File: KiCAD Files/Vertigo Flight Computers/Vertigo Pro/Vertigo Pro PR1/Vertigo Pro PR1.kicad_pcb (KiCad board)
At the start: 4 copper layers, 45.2 x 81.8 mm, 151 parts, among them IC1 ICM-20602, IC2 DPS310XTSA1, J1 ST-LINK Conn, J2 USB_C_2.0, J3 FFC2A32-24-T, J4 Screw_Terminal, J5 Screw_Terminal, J6 Screw_Terminal, J7 Screw_Terminal, Q1 MMBT3904-TP, Q2 MMBT3904-TP, Q3 FDN339AN, Q4 FDN339AN, Q5 SI7149ADP-T1-GE3, Q6 MMBT3904-TP, Q7 MMBT3904-TP, Q8 FDN339AN, Q9 FDN339AN, SW1 SW_SPDT, U1 STM32F103C8Tx, U10 TPS79133DBVR, U12 TLV709, U13 TLV75528PDBV, U2 AP63203WU, U3 ESP32-S3-WROOM-1, U4 TLV75515PDBV, U5 TLV709, U8 NEO-6M-GPS, U9 24AA32A-I_MS, Y1 16MHz

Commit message: Via fix + UART
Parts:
- moved C33 1.03 mm to (144.5, 118.0)
- moved C7 0.26 mm to (142.3, 123.7)
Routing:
- net /ESP_I2C_SCL: track 94.4 -> 84.3 mm, vias 8 -> 7
- net /CONTI_C3: track 30.0 -> 35.3 mm, vias 1 -> 2
- net AGND: track 76.0 -> 80.6 mm, vias 97 -> 95
- net /ULN_3V3: track 31.0 -> 34.0 mm, vias 5 -> 6
- net /STM_UART2_RX: track 26.8 -> 24.5 mm
- net /CONTI_C1: track 25.7 -> 27.9 mm
- net /IGN_4: track 28.8 -> 29.9 mm
- net /CONTI_C4: track 28.5 -> 29.5 mm
- net +3.3V: track 110.1 -> 109.3 mm
- net Net-(Q6-B): track 15.7 -> 16.2 mm
- net /IGN_3: track 47.4 -> 47.6 mm, vias 1 -> 2
- net /ESP_I2C_SDA: track 82.3 -> 82.5 mm, vias 8 -> 7
- net VCC: vias 14 -> 15

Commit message: Via fix, est
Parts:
- removed BOOT, RST: Jumper_2_Open, Jumper:SolderJumper-2_P1.3mm_Open_TrianglePad1.0x1.5mm
- added JP1: Jumper_2_Open, Jumper:SolderJumper-2_P1.3mm_Open_TrianglePad1.0x1.5mm, B.Cu at (151.2, 78.2)
- added JP2: Jumper_2_Open, Jumper:SolderJumper-2_P1.3mm_Open_TrianglePad1.0x1.5mm, B.Cu at (154.1, 78.2)
- moved C34 0.57 mm to (145.5, 117.0)
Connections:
- AE1 pad 2: AGND -> (no net)
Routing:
- net /ULN_3V3: track 34.0 -> 30.8 mm
- net /STM_UART2_TX: track 39.2 -> 36.1 mm
- net +3.3V: track 109.3 -> 107.1 mm, vias 54 -> 53
- net /ESP_I2C_SCL: track 84.3 -> 85.5 mm
- net /ESP_I2C_SDA: track 82.5 -> 83.3 mm
- net AGND: track 80.6 -> 80.5 mm, vias 95 -> 94

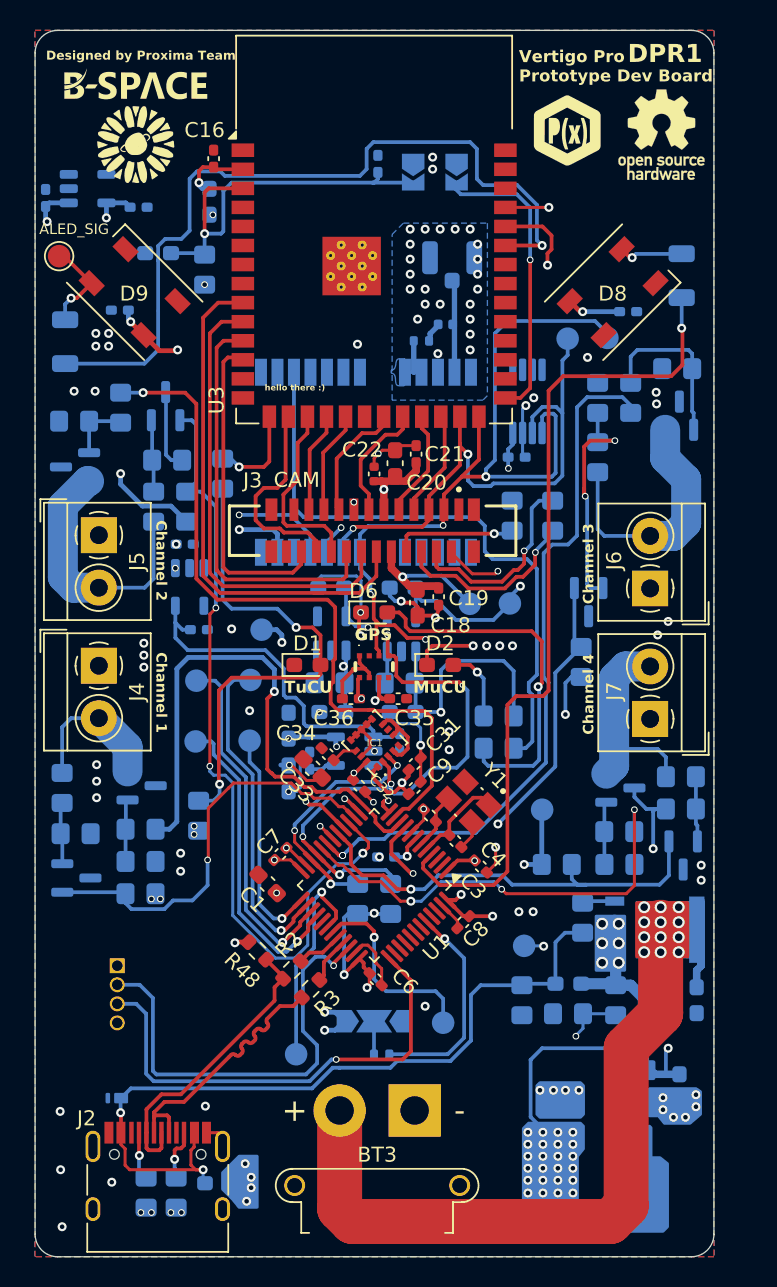
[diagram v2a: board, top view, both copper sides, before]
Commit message: internal layers clean
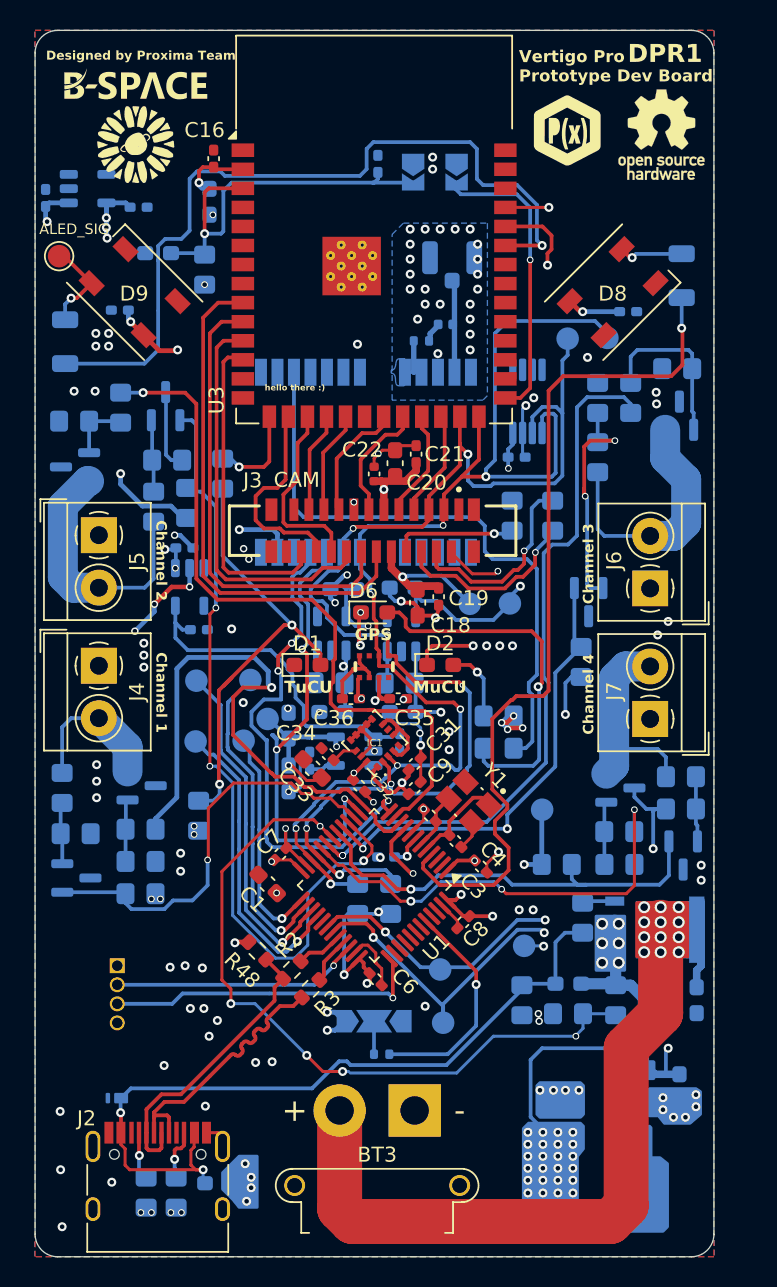
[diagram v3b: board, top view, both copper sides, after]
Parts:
- moved UART1_RX 11.1 mm to (153.0, 131.3)
- moved ULN 5.96 mm to (141.5, 114.7)
- moved C24 0.82 mm to (146.6, 106.0)
- moved NSS 0.40 mm to (139.9, 116.1)
- moved C10 0.25 mm to (135.9, 103.2)
- moved R11 0.25 mm to (136.1, 100.2)
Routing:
- net /BATT_U: track 34.4 -> 48.1 mm, vias 2 -> 5
- net /SWDIO: track 29.9 -> 16.5 mm
- net /ESP_UART_RX: track 79.4 -> 67.6 mm, vias 2 -> 3
- net /SWCLK: track 31.7 -> 21.5 mm
- net /ULN_3V3: track 30.8 -> 20.7 mm, vias 6 -> 4
- net /STM_UART2_RX: track 24.5 -> 32.3 mm, vias 2 -> 3
- net AGND: track 80.5 -> 87.8 mm, vias 94 -> 116
- net +3.3V: track 107.1 -> 99.9 mm, vias 53 -> 57
- net /CONTI_C3: track 35.3 -> 30.5 mm
- net /ESP_UART_TX: track 79.1 -> 75.2 mm, vias 2 -> 3
- net Net-(D1-A): track 33.3 -> 30.4 mm
- net /ALED_PWR: track 61.2 -> 63.9 mm, vias 4 -> 6
- net /ESP_I2C_SDA: track 83.3 -> 85.7 mm
- net /STM_UART2_TX: track 36.1 -> 33.8 mm, vias 2 -> 3
- net /IGN_1: track 36.9 -> 38.9 mm
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
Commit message: BATT_U trace fix, est, via fix
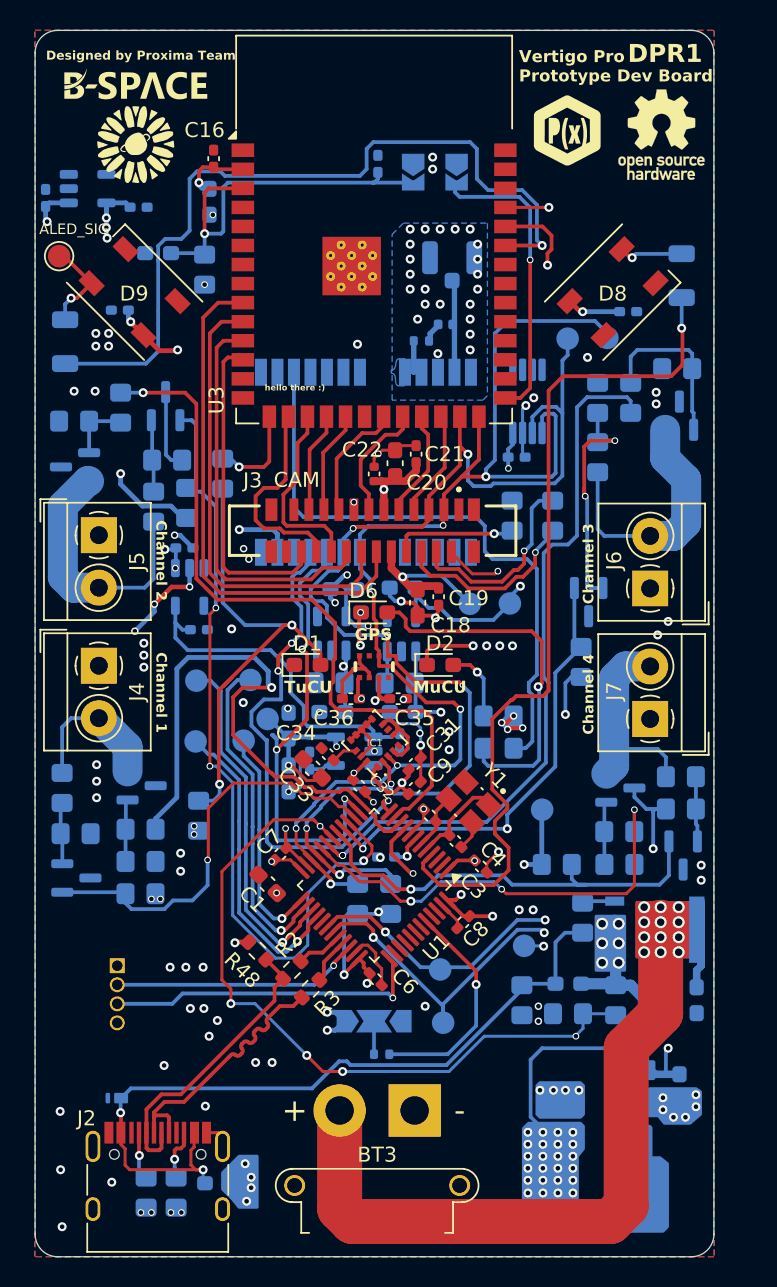
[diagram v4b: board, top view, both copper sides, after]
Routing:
- net Net-(D1-A): track 30.4 -> 32.2 mm
- net /ESP_I2C_SDA: track 85.7 -> 84.7 mm
- net /STM_SPI_MISO: track 22.9 -> 23.5 mm

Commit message: Routing fix
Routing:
- net AGND: track 87.8 -> 87.7 mm, vias 116 -> 117
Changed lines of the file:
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@@
 	)
 	(segment
+		(start 146.4825 112.112095)
+		(end 146.4825 113.3)
+		(width 0.25)
+		(layer "F.Cu")
+		(net 59)
+	)
+	(segment
 		(start 147.725 107.55)
 		(end 147.725 107.55)
@@
 	)
 	(segment
-		(start 147.212445 111.303554)
-		(end 147.175 111.340999)
-		(width 0.25)
-		(layer "F.Cu")
-		(net 59)
-	)
-	(segment
 		(start 147.7 107.55)
 		(end 147.7 107.575)
@@
 	)
 	(segment
-		(start 147.996446 111.303554)
-		(end 147.212445 111.303554)
-		(width 0.25)
-		(layer "F.Cu")
-		(net 59)
-	)
-	(segment
 		(start 147.725 107.55)
 		(end 147.7 107.55)
@@
 	)
 	(segment
-		(start 146.4825 112.112095)
-		(end 146.4825 113.3)
-		(width 0.25)
-		(layer "F.Cu")
-		(net 59)
-	)
-	(segment
 		(start 150.133074 117.033076)
 		(end 150.436844 117.033076)
@@
 	)
 	(segment
-		(start 147.175 111.419595)
-		(end 146.4825 112.112095)
-		(width 0.25)
-		(layer "F.Cu")
-		(net 59)
-	)
-	(segment
 		(start 148.325 115.932107)
 		(end 147.746446 115.353553)
@@
 	)
 	(segment
-		(start 147.175 111.340999)
-		(end 147.175 111.419595)
-		(width 0.25)
-		(layer "F.Cu")
-		(net 59)
-	)
-	(segment
 		(start 150 96.737499)
 		(end 150 96.875)
@@
 	)
 	(segment
+		(start 147.291041 111.303554)
+		(end 146.4825 112.112095)
+		(width 0.25)
+		(layer "F.Cu")
+		(net 59)
+	)
+	(segment
 		(start 148.875 96.975)
 		(end 148.875 97)
@@
 	)
 	(segment
+		(start 147.996446 111.303554)
+		(end 147.291041 111.303554)
+		(width 0.25)
+		(layer "F.Cu")
+		(net 59)
+	)
+	(segment
 		(start 138.494999 142.544999)
 		(end 138.18 142.23)
@@
 	)
 	(via
+		(at 145.45 108.95)
+		(size 0.45)
+		(drill 0.3)
+		(layers "F.Cu" "B.Cu")
+		(free yes)
+		(net 59)
+	)
+	(via
 		(at 142.7 121.95)
 		(size 0.45)
@@
 		(min_thickness 0.25)
 		(filled_areas_thickness no)
-		(fill
+		(fill yes
 			(thermal_gap 0.5)
 			(thermal_bridge_width 0.5)
@@
 		(min_thickness 0.25)
 		(filled_areas_thickness no)
-		(fill
+		(fill yes
 			(thermal_gap 0.5)
 			(thermal_bridge_width 0.5)
@@
 		(min_thickness 0.25)
 		(filled_areas_thickness no)
-		(fill
+		(fill yes
 			(thermal_gap 0.5)
 			(thermal_bridge_width 0.5)
@@
 		(min_thickness 0.0254)
 		(filled_areas_thickness no)
-		(fill
+		(fill yes
 			(thermal_gap 0.5)
 			(thermal_bridge_width 0.5)

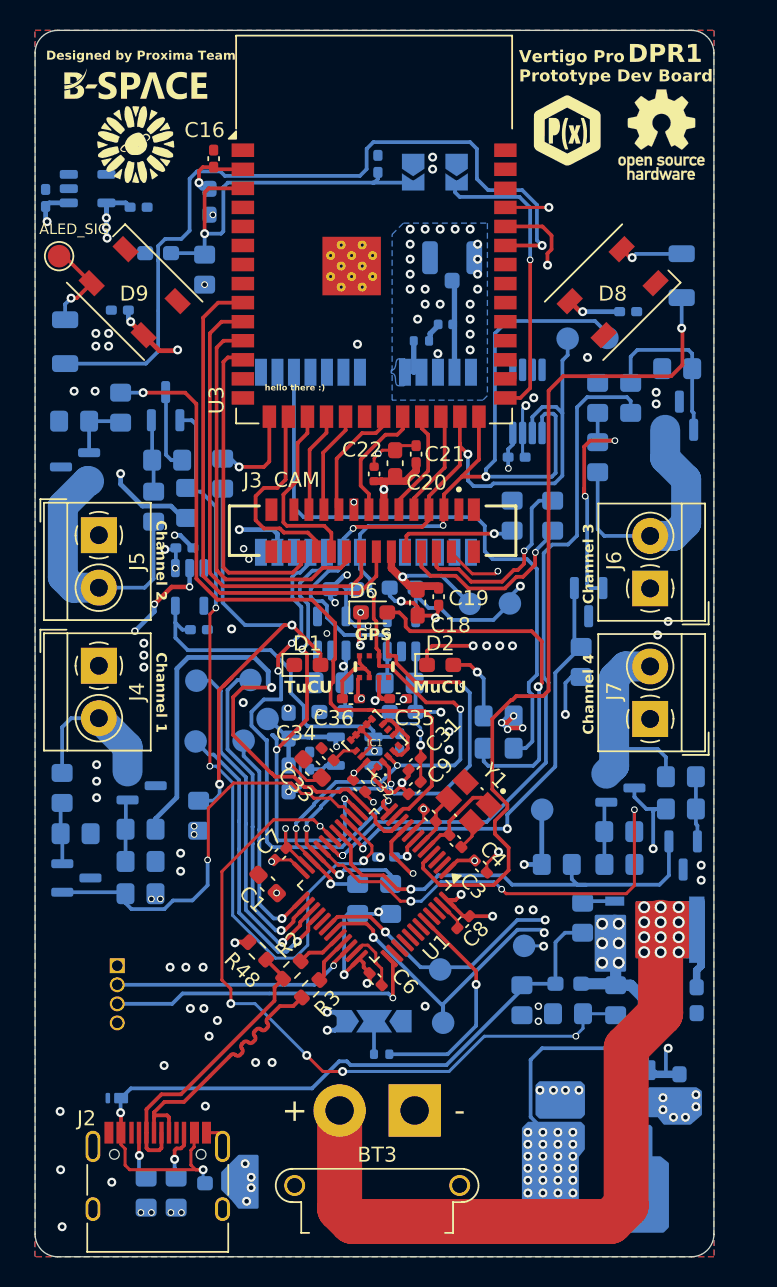
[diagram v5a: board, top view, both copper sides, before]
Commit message: Via fix, esthetics ULN, 1V5 and 2V8 test point removed
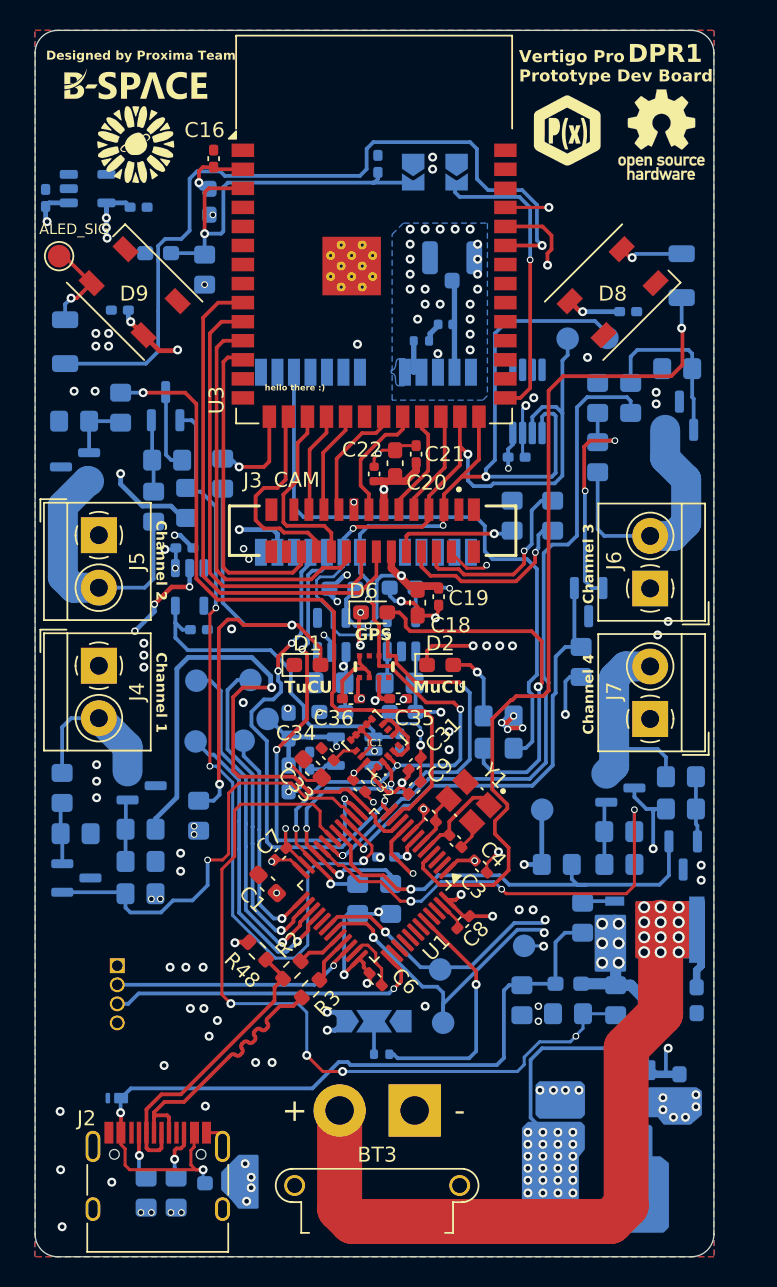
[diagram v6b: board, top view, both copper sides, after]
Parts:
- removed 1V5, 2V8: TestPoint_Pad_D1.5mm, TestPoint:TestPoint_Pad_D1.5mm
- moved U4 0.10 mm to (145.8, 109.0)
- moved C24 0.08 mm to (146.5, 106.0)
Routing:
- net /DVDD_1V5: track 24.0 -> 18.0 mm
- net /BATT_U: track 48.2 -> 53.5 mm, vias 5 -> 4
- net /AVDD_2V8: track 45.9 -> 43.1 mm
- net /USB_VBUS_D_CUTOFF: track 51.3 -> 53.8 mm
- net Net-(D1-A): track 32.2 -> 34.4 mm
- net /STM_UART2_RX: track 32.3 -> 30.4 mm
- net /ALED_PWR: track 63.9 -> 65.5 mm
- net /ESP_UART_TX: track 75.2 -> 76.6 mm
- net /STM_UART2_TX: track 33.7 -> 32.4 mm
- net /IGN_1: track 38.9 -> 40.2 mm
- net /BOOT0: track 14.9 -> 16.1 mm
- net /CONTI_C2: track 55.0 -> 55.8 mm
- net /CONTI_C1: track 27.7 -> 28.4 mm
- net /CONTI_C3: track 30.5 -> 30.4 mm, vias 2 -> 1

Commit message: esthetics
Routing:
- net AGND: track 88.2 -> 77.6 mm
- net /STM_ALED: track 57.7 -> 57.0 mm
- net /BATT_U: track 53.5 -> 53.8 mm, vias 4 -> 3

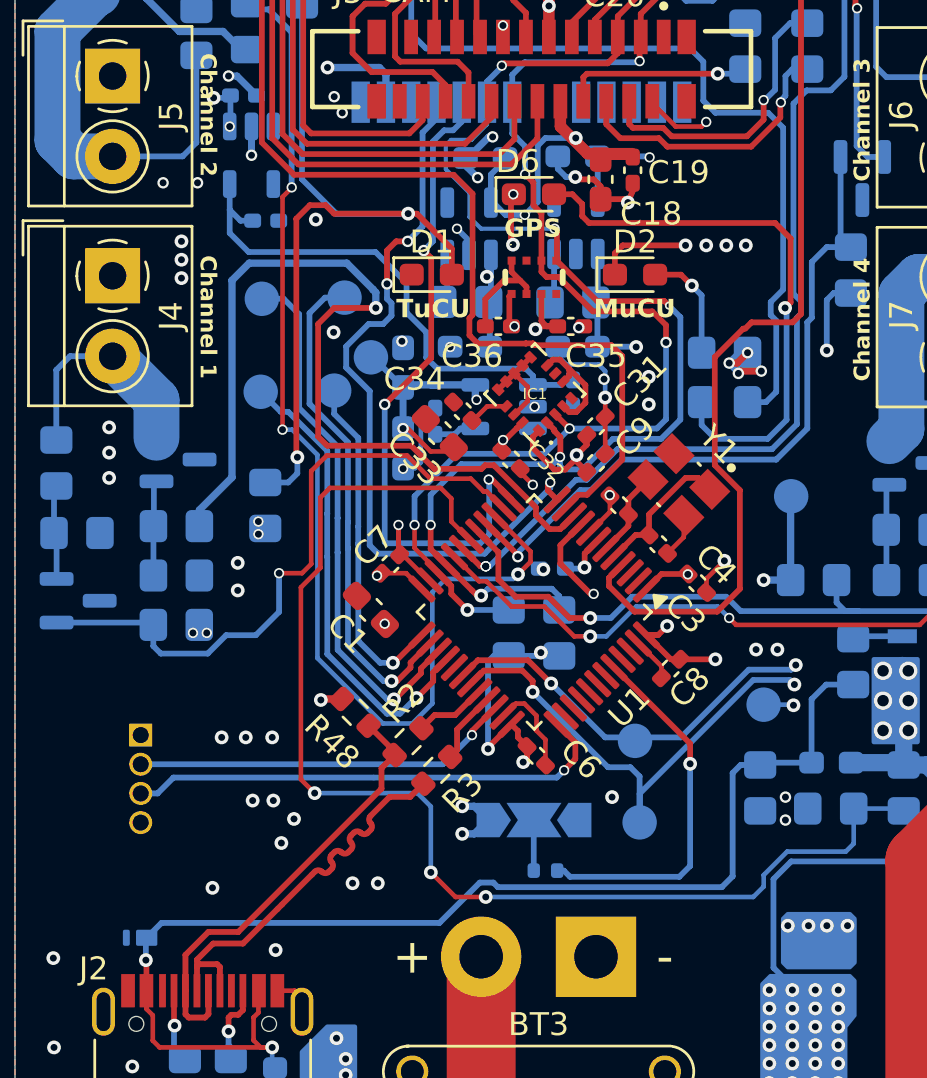
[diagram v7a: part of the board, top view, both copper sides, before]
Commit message: UART2 testpoint, silkscreen, SWD desc, esthetics + minor fixes
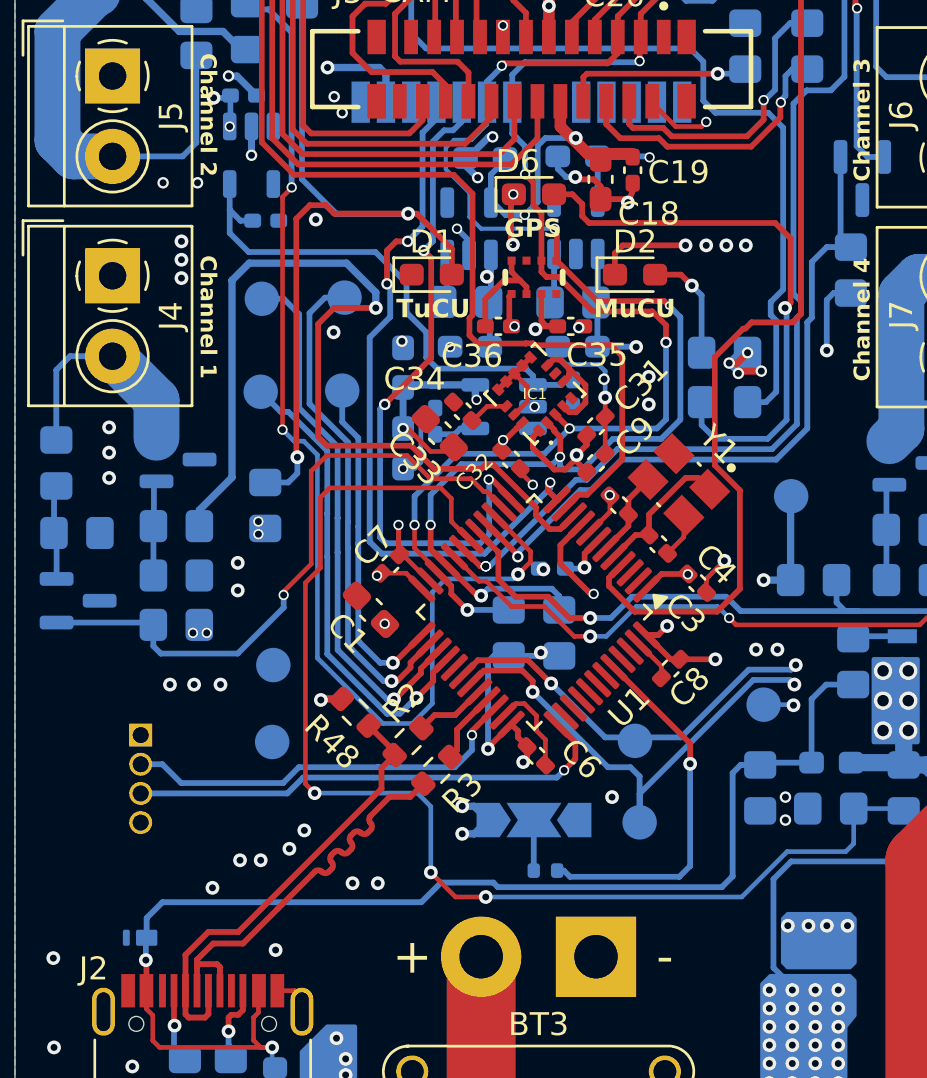
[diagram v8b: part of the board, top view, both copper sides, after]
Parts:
- removed ULN: TestPoint_Pad_D1.5mm, TestPoint:TestPoint_Pad_D1.5mm
- added UART2_RX: TestPoint_Pad_D1.5mm, TestPoint:TestPoint_Pad_D1.5mm, B.Cu at (137.2, 128.1)
- added UART2_TX: TestPoint_Pad_D1.5mm, TestPoint:TestPoint_Pad_D1.5mm, B.Cu at (137.2, 131.4)
- moved NSS 0.35 mm to (140.2, 116.1)
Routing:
- net /ULN_3V3: track 20.7 -> 18.2 mm
- net /STM_UART2_TX: track 32.7 -> 31.3 mm
- net /SWDIO: track 16.5 -> 17.6 mm
- net /CONTI_C1: track 28.4 -> 27.8 mm
- net /USB_VBUS_D_CUTOFF: track 53.8 -> 54.3 mm
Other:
- board text added: "+3.3V"
- board text added: "3V3"
- board text added: "BOOT"
- board text added: "GND"
- board text added: "RST"
- board text added: "SWCLK"
- board text added: "SWD"
- board text added: "SWDIO"
